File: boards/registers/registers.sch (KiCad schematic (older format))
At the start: 42 parts, among them U1 SN74ACT08PW, U2 SN74ACT244PW, U3 MC74AC273DTR2G, U4 MC74ACT161DG

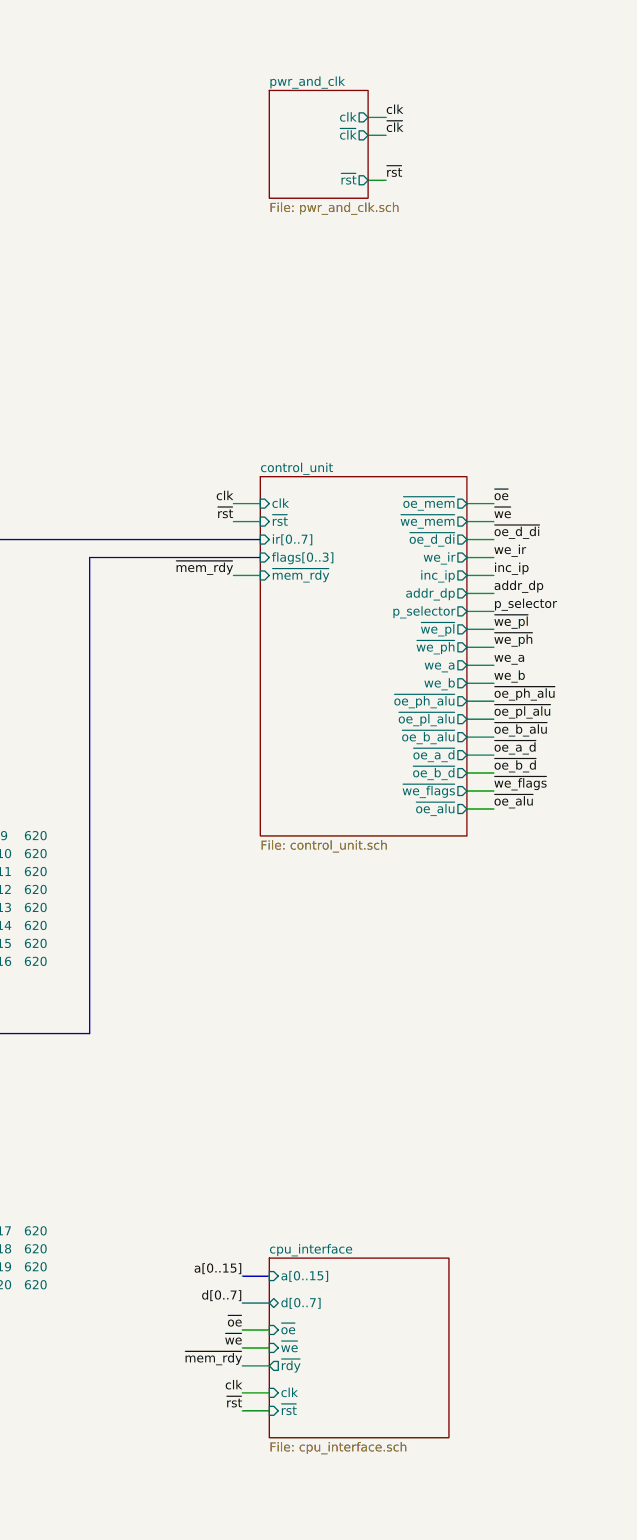
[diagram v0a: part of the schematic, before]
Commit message: Registers: new clock and reset
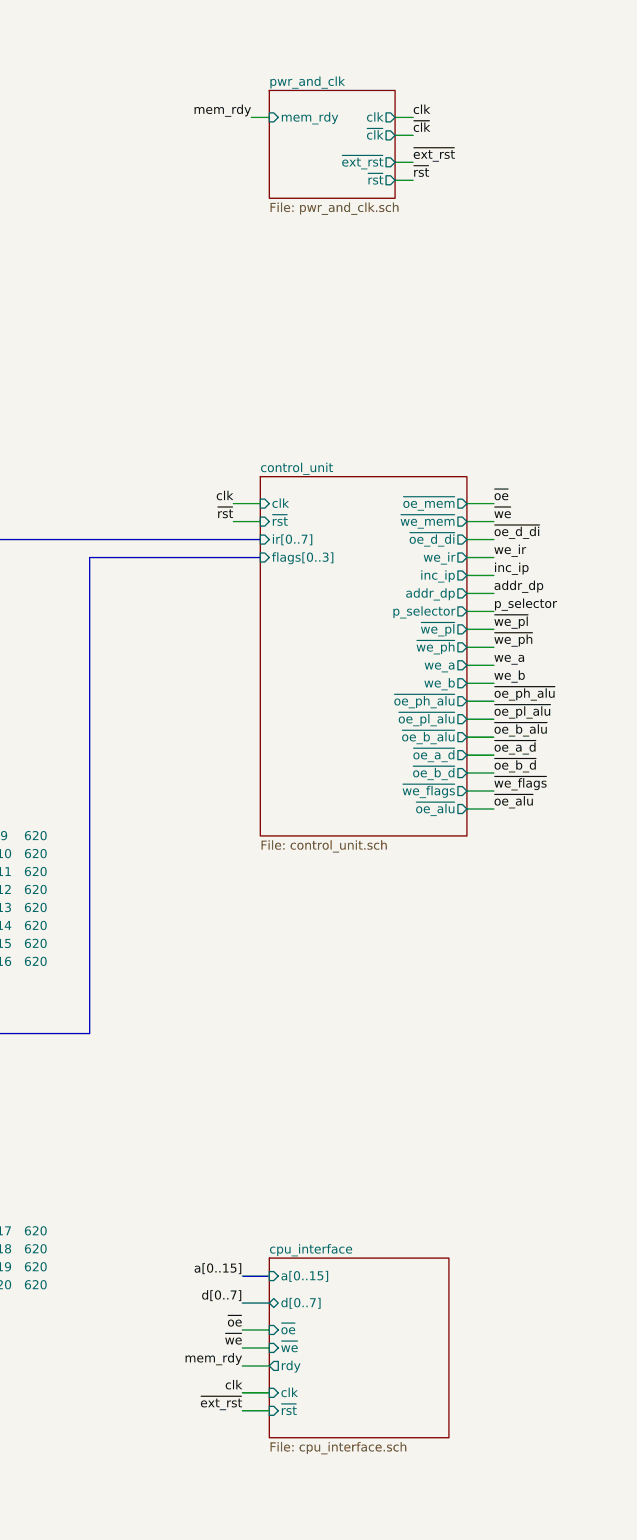
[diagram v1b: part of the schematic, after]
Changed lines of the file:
@@
 Sheet 1 10
 Title "CPU registers and memory module"
-Date "2019-12-28"
-Rev "1"
+Date "2021-01-18"
+Rev "2"
 Comp ""
 Comment1 "Licensed under the TAPR Open Hardware License (www.tapr.org/OHL)"
@@
 F4 "ir[0..7]" I L 7450 3450 50
 F5 "flags[0..3]" I L 7450 3550 50
-F6 "~mem_rdy" I L 7450 3650 50
-F7 "~oe_mem" O R 8600 3250 50
-F8 "~we_mem" O R 8600 3350 50
-F9 "~oe_d_di" O R 8600 3450 50
-F10 "we_ir" O R 8600 3550 50
-F11 "inc_ip" O R 8600 3650 50
-F12 "addr_dp" O R 8600 3750 50
-F13 "~we_pl" O R 8600 3950 50
-F14 "~we_ph" O R 8600 4050 50
-F15 "we_a" O R 8600 4150 50
-F16 "we_b" O R 8600 4250 50
-F17 "~oe_ph_alu" O R 8600 4350 50
-F18 "~oe_pl_alu" O R 8600 4450 50
-F19 "~oe_a_d" O R 8600 4650 50
-F20 "~oe_b_d" O R 8600 4750 50
-F21 "~we_flags" O R 8600 4850 50
-F22 "~oe_alu" O R 8600 4950 50
-F23 "~oe_b_alu" O R 8600 4550 50
-F24 "p_selector" O R 8600 3850 50
+F6 "~oe_mem" O R 8600 3250 50
+F7 "~we_mem" O R 8600 3350 50
+F8 "~oe_d_di" O R 8600 3450 50
+F9 "we_ir" O R 8600 3550 50
+F10 "inc_ip" O R 8600 3650 50
+F11 "addr_dp" O R 8600 3750 50
+F12 "~we_pl" O R 8600 3950 50
+F13 "~we_ph" O R 8600 4050 50
+F14 "we_a" O R 8600 4150 50
+F15 "we_b" O R 8600 4250 50
+F16 "~oe_ph_alu" O R 8600 4350 50
+F17 "~oe_pl_alu" O R 8600 4450 50
+F18 "~oe_a_d" O R 8600 4650 50
+F19 "~oe_b_d" O R 8600 4750 50
+F20 "~we_flags" O R 8600 4850 50
+F21 "~oe_alu" O R 8600 4950 50
+F22 "~oe_b_alu" O R 8600 4550 50
+F23 "p_selector" O R 8600 3850 50
 $EndSheet
 Wire Wire Line
@@
 Wire Wire Line
 	7450 3350 7300 3350
-Wire Wire Line
-	7450 3650 7300 3650
 Wire Wire Line
 	8600 3250 8750 3250
@@
 Wire Bus Line
 	6500 3550 7450 3550
-Text Label 7300 3650 2    50   ~ 0
-~mem_rdy
 Text Label 8750 3250 0    50   ~ 0
 ~oe
@@
 F4 "~oe" I L 7500 7850 50
 F5 "~we" I L 7500 7950 50
-F6 "~rdy" O L 7500 8050 50
-F7 "clk" I L 7500 8200 50
-F8 "~rst" I L 7500 8300 50
+F6 "clk" I L 7500 8200 50
+F7 "~rst" I L 7500 8300 50
+F8 "rdy" O L 7500 8050 50
 $EndSheet
 Wire Bus Line
@@
 clk
 Text Label 7350 8300 2    50   ~ 0
-~rst
+~ext_rst
 Text Label 7350 8050 2    50   ~ 0
-~mem_rdy
+mem_rdy
 Text Label 7350 7850 2    50   ~ 0
 ~oe
 Text Label 7350 7950 2    50   ~ 0
 ~we
-$Sheet
-S 7500 950  550  600
-U 5EF05415
-F0 "pwr_and_clk" 50
-F1 "pwr_and_clk.sch" 50
-F2 "clk" O R 8050 1100 50
-F3 "~rst" O R 8050 1450 50
-F4 "~clk" O R 8050 1200 50
-$EndSheet
-Wire Wire Line
-	8050 1100 8150 1100
-Wire Wire Line
-	8150 1200 8050 1200
-Wire Wire Line
-	8150 1450 8050 1450
-Text Label 8150 1100 0    50   ~ 0
+Text Label 8300 1100 0    50   ~ 0
 clk
-Text Label 8150 1200 0    50   ~ 0
+Text Label 8300 1200 0    50   ~ 0
 ~clk
-Text Label 8150 1450 0    50   ~ 0
+Text Label 8300 1450 0    50   ~ 0
 ~rst
 Wire Bus Line
@@
 $EndComp
 NoConn ~ 2950 10600
+$Sheet
+S 7500 950  700  600
+U 5EF05415
+F0 "pwr_and_clk" 50
+F1 "pwr_and_clk.sch" 50
+F2 "clk" O R 8200 1100 50
+F3 "~rst" O R 8200 1450 50
+F4 "~clk" O R 8200 1200 50
+F5 "~ext_rst" O R 8200 1350 50
+F6 "mem_rdy" I L 7500 1100 50
+$EndSheet
+Wire Wire Line
+	8300 1450 8200 1450
+Wire Wire Line
+	8300 1200 8200 1200
+Wire Wire Line
+	8200 1100 8300 1100
+Text Label 8300 1350 0    50   ~ 0
+~ext_rst
+Wire Wire Line
+	8300 1350 8200 1350
+Text Label 7400 1100 2    50   ~ 0
+mem_rdy
+Wire Wire Line
+	7400 1100 7500 1100
 Wire Bus Line
 	13750 4550 13750 5950

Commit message: Registers: more decoupling capacitors
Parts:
- added C5, C7: 0.1u, Capacitor_SMD:C_0805_2012Metric, symbol Device:C
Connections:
- net GND: now also C5.2, C7.2
- net VCC: now also C5.1, C7.1
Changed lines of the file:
@@
 Wire Wire Line
 	7400 1100 7500 1100
+$Comp
+L Device:C C7
+U 1 1 6011F1FA
+P 4000 7850
+F 0 "C7" H 4115 7896 50  0000 L CNN
+F 1 "0.1u" H 4115 7805 50  0000 L CNN
+F 2 "Capacitor_SMD:C_0805_2012Metric" H 4038 7700 50  0001 C CNN
+F 3 "~" H 4000 7850 50  0001 C CNN
+	1    4000 7850
+	1    0    0    -1
+$EndComp
+$Comp
+L power:VCC #PWR0148
+U 1 1 6011F200
+P 4000 7700
+F 0 "#PWR0148" H 4000 7550 50  0001 C CNN
+F 1 "VCC" H 4017 7873 50  0000 C CNN
+F 2 "" H 4000 7700 50  0001 C CNN
+F 3 "" H 4000 7700 50  0001 C CNN
+	1    4000 7700
+	1    0    0    -1
+$EndComp
+$Comp
+L power:GND #PWR0149
+U 1 1 6011F206
+P 4000 8000
+F 0 "#PWR0149" H 4000 7750 50  0001 C CNN
+F 1 "GND" H 4005 7827 50  0000 C CNN
+F 2 "" H 4000 8000 50  0001 C CNN
+F 3 "" H 4000 8000 50  0001 C CNN
+	1    4000 8000
+	1    0    0    -1
+$EndComp
+$Comp
+L Device:C C5
+U 1 1 6012815C
+P 1650 10050
+F 0 "C5" H 1765 10096 50  0000 L CNN
+F 1 "0.1u" H 1765 10005 50  0000 L CNN
+F 2 "Capacitor_SMD:C_0805_2012Metric" H 1688 9900 50  0001 C CNN
+F 3 "~" H 1650 10050 50  0001 C CNN
+	1    1650 10050
+	1    0    0    -1
+$EndComp
+$Comp
+L power:VCC #PWR0100
+U 1 1 60128162
+P 1650 9900
+F 0 "#PWR0100" H 1650 9750 50  0001 C CNN
+F 1 "VCC" H 1667 10073 50  0000 C CNN
+F 2 "" H 1650 9900 50  0001 C CNN
+F 3 "" H 1650 9900 50  0001 C CNN
+	1    1650 9900
+	1    0    0    -1
+$EndComp
+$Comp
+L power:GND #PWR0139
+U 1 1 60128168
+P 1650 10200
+F 0 "#PWR0139" H 1650 9950 50  0001 C CNN
+F 1 "GND" H 1655 10027 50  0000 C CNN
+F 2 "" H 1650 10200 50  0001 C CNN
+F 3 "" H 1650 10200 50  0001 C CNN
+	1    1650 10200
+	1    0    0    -1
+$EndComp
 Wire Bus Line
 	13750 4550 13750 5950

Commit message: Registers: change logic family to HC and LV-A
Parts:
- U1: value SN74ACT08PW -> SN74LV08APW
- U2: value SN74ACT244PW -> MC74HC244ADT
- U3: value MC74AC273DTR2G -> MC74HC273ADT
- U4: value MC74ACT161DG -> 74HC161PW; footprint Package_SO:SOIC-16_3.9x9.9mm_P1.27mm -> Package_SO:TSSOP-16_4.4x5mm_P0.65mm
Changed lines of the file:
@@
 P 3350 4150
 F 0 "U3" H 3750 3600 50  0000 C CNN
-F 1 "MC74AC273DTR2G" H 3800 3500 50  0000 C CNN
+F 1 "MC74HC273ADT" H 3800 3500 50  0000 C CNN
 F 2 "Package_SO:TSSOP-20_4.4x6.5mm_P0.65mm" H 3350 4150 50  0001 C CNN
-F 3 "https://assets.nexperia.com/documents/data-sheet/74HC_HCT273.pdf" H 3350 4150 50  0001 C CNN
+F 3 "http://www.farnell.com/datasheets/1878567.pdf" H 3350 4150 50  0001 C CNN
 	1    3350 4150
 	1    0    0    -1
@@
 P 3350 1550
 F 0 "U2" H 3750 1000 50  0000 C CNN
-F 1 "SN74ACT244PW" H 3650 900 50  0000 C CNN
+F 1 "MC74HC244ADT" H 3650 900 50  0000 C CNN
 F 2 "Package_SO:TSSOP-20_4.4x6.5mm_P0.65mm" H 3350 1550 50  0001 C CNN
-F 3 "https://assets.nexperia.com/documents/data-sheet/74HC_HCT244.pdf" H 3350 1550 50  0001 C CNN
+F 3 "http://www.farnell.com/datasheets/1878565.pdf" H 3350 1550 50  0001 C CNN
 	1    3350 1550
 	1    0    0    -1
@@
 P 2100 5350
 F 0 "U1" H 2100 5675 50  0000 C CNN
-F 1 "SN74ACT08PW" H 2100 5584 50  0000 C CNN
+F 1 "SN74LV08APW" H 2100 5584 50  0000 C CNN
 F 2 "Package_SO:TSSOP-14_4.4x5mm_P0.65mm" H 2100 5350 50  0001 C CNN
-F 3 "http://www.ti.com/lit/gpn/sn74LS08" H 2100 5350 50  0001 C CNN
+F 3 "https://www.ti.com/lit/ds/symlink/sn74lv08a.pdf" H 2100 5350 50  0001 C CNN
 	1    2100 5350
 	1    0    0    -1
@@
 P 10300 3450
 F 0 "U1" H 10300 3775 50  0000 C CNN
-F 1 "SN74ACT08PW" H 10300 3684 50  0000 C CNN
+F 1 "SN74LV08APW" H 10300 3684 50  0000 C CNN
 F 2 "Package_SO:TSSOP-14_4.4x5mm_P0.65mm" H 10300 3450 50  0001 C CNN
-F 3 "http://www.ti.com/lit/gpn/sn74LS08" H 10300 3450 50  0001 C CNN
+F 3 "https://www.ti.com/lit/ds/symlink/sn74lv08a.pdf" H 10300 3450 50  0001 C CNN
 	2    10300 3450
 	1    0    0    -1
@@
 P 10300 5050
 F 0 "U1" H 10300 5375 50  0000 C CNN
-F 1 "SN74ACT08PW" H 10300 5284 50  0000 C CNN
+F 1 "SN74LV08APW" H 10300 5284 50  0000 C CNN
 F 2 "Package_SO:TSSOP-14_4.4x5mm_P0.65mm" H 10300 5050 50  0001 C CNN
-F 3 "http://www.ti.com/lit/gpn/sn74LS08" H 10300 5050 50  0001 C CNN
+F 3 "https://www.ti.com/lit/ds/symlink/sn74lv08a.pdf" H 10300 5050 50  0001 C CNN
 	3    10300 5050
 	1    0    0    -1
@@
 P 1000 10500
 F 0 "U1" H 1230 10546 50  0000 L CNN
-F 1 "SN74ACT08PW" H 1230 10455 50  0000 L CNN
+F 1 "SN74LV08APW" H 1230 10455 50  0000 L CNN
 F 2 "Package_SO:TSSOP-14_4.4x5mm_P0.65mm" H 1000 10500 50  0001 C CNN
-F 3 "http://www.ti.com/lit/gpn/sn74LS08" H 1000 10500 50  0001 C CNN
+F 3 "https://www.ti.com/lit/ds/symlink/sn74lv08a.pdf" H 1000 10500 50  0001 C CNN
 	5    1000 10500
 	1    0    0    -1
@@
 P 3350 6800
 F 0 "U4" H 3750 6250 50  0000 C CNN
-F 1 "MC74ACT161DG" H 3650 6150 50  0000 C CNN
-F 2 "Package_SO:SOIC-16_3.9x9.9mm_P1.27mm" H 3350 6800 50  0001 C CNN
-F 3 "http://www.ti.com/lit/gpn/sn74LS161" H 3350 6800 50  0001 C CNN
+F 1 "74HC161PW" H 3650 6150 50  0000 C CNN
+F 2 "Package_SO:TSSOP-16_4.4x5mm_P0.65mm" H 3350 6800 50  0001 C CNN
+F 3 "http://www.farnell.com/datasheets/308767.pdf" H 3350 6800 50  0001 C CNN
 	1    3350 6800
 	1    0    0    -1
@@
 P 2650 10600
 F 0 "U1" H 2650 10925 50  0000 C CNN
-F 1 "SN74ACT08PW" H 2650 10834 50  0000 C CNN
+F 1 "SN74LV08APW" H 2650 10834 50  0000 C CNN
 F 2 "Package_SO:TSSOP-14_4.4x5mm_P0.65mm" H 2650 10600 50  0001 C CNN
-F 3 "http://www.ti.com/lit/gpn/sn74LS08" H 2650 10600 50  0001 C CNN
+F 3 "https://www.ti.com/lit/ds/symlink/sn74lv08a.pdf" H 2650 10600 50  0001 C CNN
 	4    2650 10600
 	1    0    0    -1

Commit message: Registers: new board started
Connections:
- net GND: no longer U1.12, U1.13
- net VCC: now also U1.12, U1.13
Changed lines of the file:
@@
 	1    0    0    -1
-$EndComp
-$Comp
-L power:GND #PWR08
-U 1 1 6058DCB0
-P 2350 10500
-F 0 "#PWR08" H 2350 10250 50  0001 C CNN
-F 1 "GND" H 2355 10327 50  0000 C CNN
-F 2 "" H 2350 10500 50  0001 C CNN
-F 3 "" H 2350 10500 50  0001 C CNN
-	1    2350 10500
-	0    1    1    0
-$EndComp
-$Comp
-L power:GND #PWR09
-U 1 1 6058E349
-P 2350 10700
-F 0 "#PWR09" H 2350 10450 50  0001 C CNN
-F 1 "GND" H 2355 10527 50  0000 C CNN
-F 2 "" H 2350 10700 50  0001 C CNN
-F 3 "" H 2350 10700 50  0001 C CNN
-	1    2350 10700
-	0    1    1    0
 $EndComp
 NoConn ~ 2950 10600
@@
 	1    0    0    -1
 $EndComp
+$Comp
+L power:VCC #PWR0133
+U 1 1 60242527
+P 2350 10600
+F 0 "#PWR0133" H 2350 10450 50  0001 C CNN
+F 1 "VCC" H 2367 10773 50  0000 C CNN
+F 2 "" H 2350 10600 50  0001 C CNN
+F 3 "" H 2350 10600 50  0001 C CNN
+	1    2350 10600
+	0    -1   -1   0
+$EndComp
+Wire Wire Line
+	2350 10500 2350 10600
+Connection ~ 2350 10600
+Wire Wire Line
+	2350 10600 2350 10700
 Wire Bus Line
 	13750 4550 13750 5950
